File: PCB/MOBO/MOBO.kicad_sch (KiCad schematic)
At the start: 11 parts, among them J10 COMP_OUT, J103 RPi_GPio, J104 RPi_GND, J105 RPi_5V, J106 RPi_DM, J107 RPi_DM, J11 COMP_5V, J12 COMP_GND, J7 RPi_TV, J8 RPi_SDA0, J9 RPi_SCL0

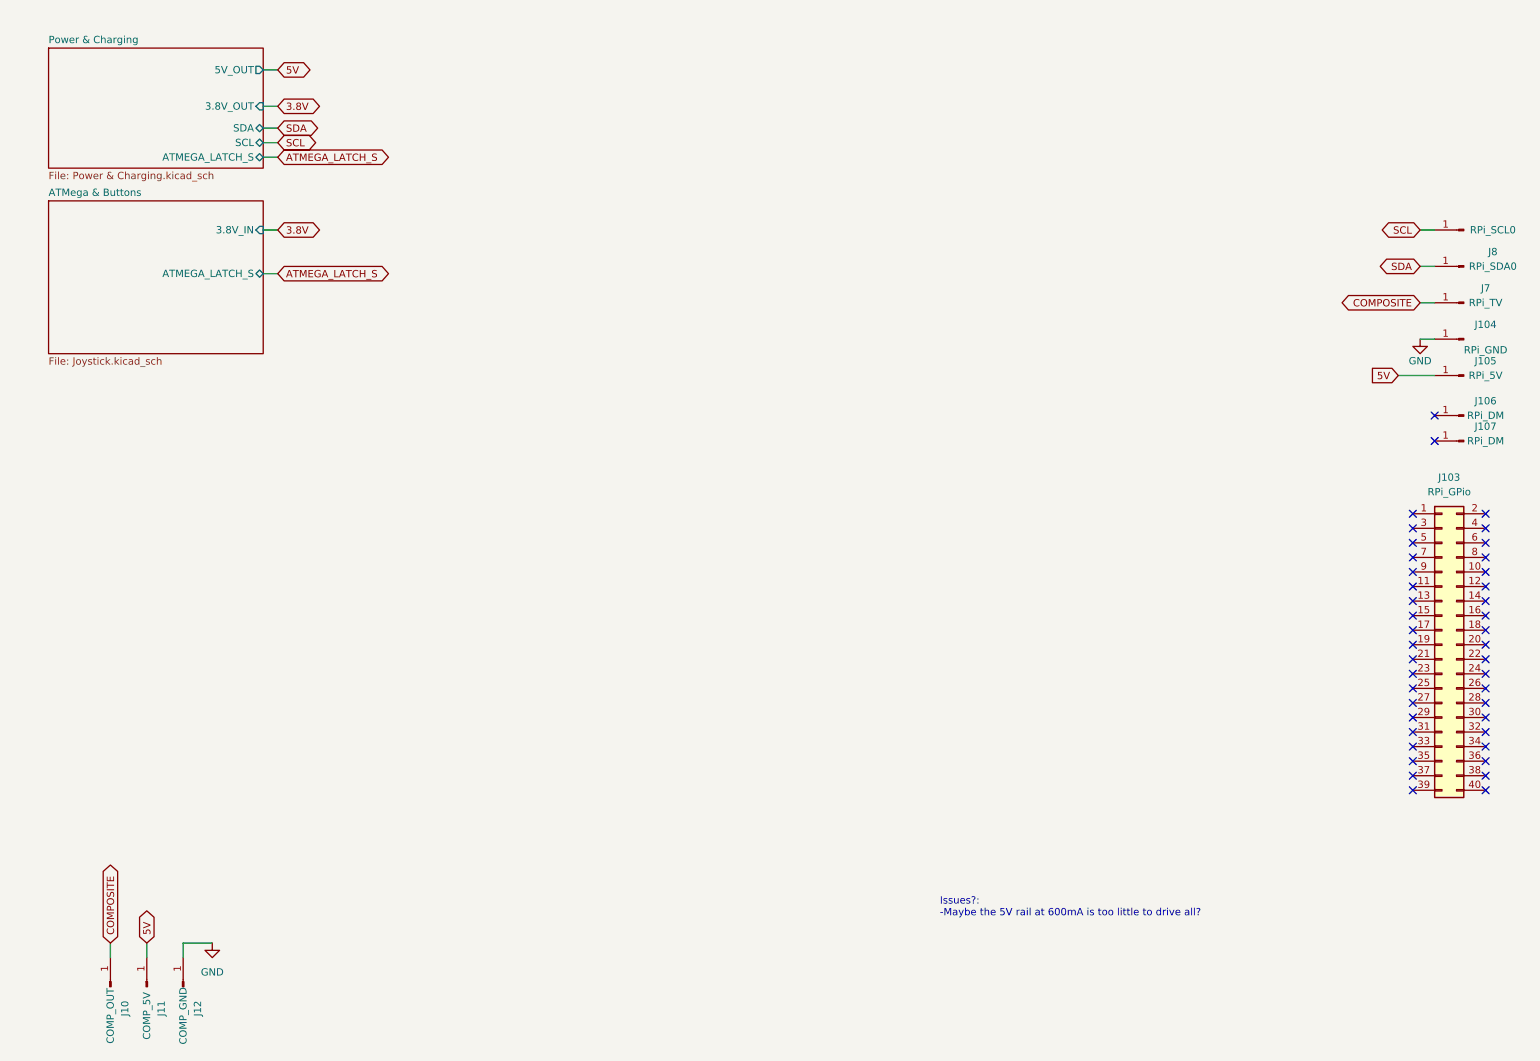
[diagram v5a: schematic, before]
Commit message: relaced usbc port schematic to add data lines
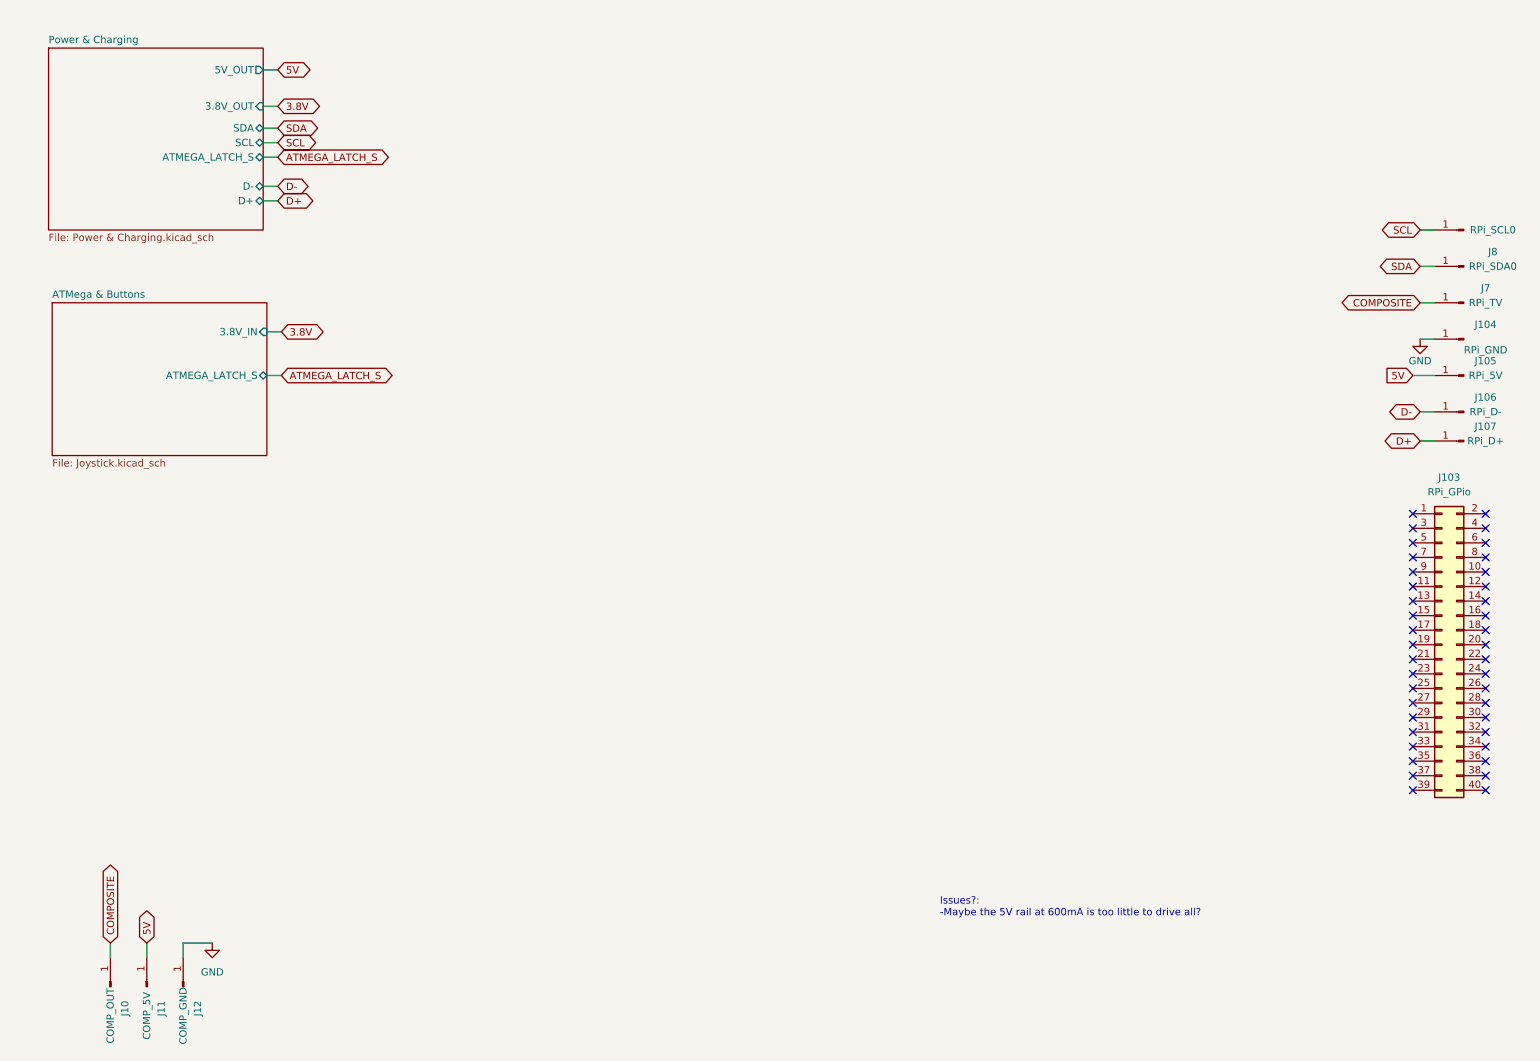
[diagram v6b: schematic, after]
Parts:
- J106: value RPi_DM -> RPi_D-
- J107: value RPi_DM -> RPi_D+
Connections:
- net D+: now reaches J107.1 (Pin_1)
- net D-: now reaches J106.1 (Pin_1)
- no-connect marks 42 -> 40
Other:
- sheet Power & Charging ports: added D+, D-; removed none
- moved on the sheet: J106
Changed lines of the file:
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@@
   (no_connect (at 260.35 107.95))
   (no_connect (at 260.35 135.89))
-  (no_connect (at 264.16 87.63))
   (no_connect (at 273.05 135.89))
   (no_connect (at 260.35 125.73))
@@
   (no_connect (at 260.35 146.05))
   (no_connect (at 260.35 113.03))
-  (no_connect (at 264.16 83.185))
   (no_connect (at 260.35 143.51))
   (no_connect (at 260.35 140.97))
@@
     (stroke (width 0) (type default))
   )
-  (wire (pts (xy 59.69 58.42) (xy 62.23 58.42))
+  (wire (pts (xy 60.325 76.2) (xy 62.865 76.2))
+    (stroke (width 0) (type default))
+  )
+  (wire (pts (xy 59.69 43.18) (xy 62.23 43.18))
+    (stroke (width 0) (type default))
+  )
+  (wire (pts (xy 264.16 87.63) (xy 261.62 87.63))
     (stroke (width 0) (type default))
   )
@@
     (stroke (width 0) (type default))
   )
+  (wire (pts (xy 264.16 82.55) (xy 261.62 82.55))
+    (stroke (width 0) (type default))
+  )
+  (wire (pts (xy 59.69 45.72) (xy 62.23 45.72))
+    (stroke (width 0) (type default))
+  )
   (wire (pts (xy 45.72 175.26) (xy 45.72 177.8))
     (stroke (width 0) (type default))
@@
     (stroke (width 0) (type default))
   )
-  (wire (pts (xy 59.69 50.8) (xy 62.23 50.8))
-    (stroke (width 0) (type default))
-  )
-  (wire (pts (xy 257.81 76.2) (xy 264.16 76.2))
+  (wire (pts (xy 260.35 76.2) (xy 264.16 76.2))
+    (stroke (width 0) (type default))
+  )
+  (wire (pts (xy 60.325 68.58) (xy 62.865 68.58))
     (stroke (width 0) (type default))
   )
@@
     )
   )
-  (global_label "ATMEGA_LATCH_S" (shape bidirectional) (at 62.23 58.42 0) (fields_autoplaced)
-    (effects (font (size 1.27 1.27)) (justify left))
-    (property "Intersheetrefs" "${INTERSHEET_REFS}" (at 82.1712 58.42 0)
+  (global_label "ATMEGA_LATCH_S" (shape bidirectional) (at 62.865 76.2 0) (fields_autoplaced)
+    (effects (font (size 1.27 1.27)) (justify left))
+    (property "Intersheetrefs" "${INTERSHEET_REFS}" (at 82.8062 76.2 0)
       (effects (font (size 1.27 1.27)) (justify left) hide)
     )
@@
     )
   )
+  (global_label "D+" (shape bidirectional) (at 62.23 45.72 0) (fields_autoplaced)
+    (effects (font (size 1.27 1.27)) (justify left))
+    (property "Intersheetrefs" "${INTERSHEET_REFS}" (at 69.1689 45.72 0)
+      (effects (font (size 1.27 1.27)) (justify left) hide)
+    )
+  )
   (global_label "COMPOSITE" (shape bidirectional) (at 33.02 175.26 90) (fields_autoplaced)
     (effects (font (size 1.27 1.27)) (justify left))
@@
     )
   )
-  (global_label "5V" (shape input) (at 257.81 76.2 180) (fields_autoplaced)
+  (global_label "5V" (shape input) (at 260.35 76.2 180) (fields_autoplaced)
     (effects (font (size 1.27 1.27)) (justify right))
-    (property "Intersheetrefs" "${INTERSHEET_REFS}" (at 252.5267 76.2 0)
+    (property "Intersheetrefs" "${INTERSHEET_REFS}" (at 255.0667 76.2 0)
       (effects (font (size 1.27 1.27)) (justify right) hide)
     )
@@
     )
   )
-  (global_label "3.8V" (shape bidirectional) (at 62.23 50.8 0) (fields_autoplaced)
-    (effects (font (size 1.27 1.27)) (justify left))
-    (property "Intersheetrefs" "${INTERSHEET_REFS}" (at 70.4389 50.8 0)
+  (global_label "3.8V" (shape bidirectional) (at 62.865 68.58 0) (fields_autoplaced)
+    (effects (font (size 1.27 1.27)) (justify left))
+    (property "Intersheetrefs" "${INTERSHEET_REFS}" (at 71.0739 68.58 0)
+      (effects (font (size 1.27 1.27)) (justify left) hide)
+    )
+  )
+  (global_label "D-" (shape bidirectional) (at 62.23 43.18 0) (fields_autoplaced)
+    (effects (font (size 1.27 1.27)) (justify left))
+    (property "Intersheetrefs" "${INTERSHEET_REFS}" (at 69.1689 43.18 0)
       (effects (font (size 1.27 1.27)) (justify left) hide)
     )
@@
     )
   )
+  (global_label "D+" (shape bidirectional) (at 261.62 87.63 180) (fields_autoplaced)
+    (effects (font (size 1.27 1.27)) (justify right))
+    (property "Intersheetrefs" "${INTERSHEET_REFS}" (at 254.6811 87.63 0)
+      (effects (font (size 1.27 1.27)) (justify right) hide)
+    )
+  )
   (global_label "SDA" (shape bidirectional) (at 62.23 33.02 0) (fields_autoplaced)
     (effects (font (size 1.27 1.27)) (justify left))
     (property "Intersheetrefs" "${INTERSHEET_REFS}" (at 69.8946 33.02 0)
       (effects (font (size 1.27 1.27)) (justify left) hide)
+    )
+  )
+  (global_label "D-" (shape bidirectional) (at 261.62 82.55 180) (fields_autoplaced)
+    (effects (font (size 1.27 1.27)) (justify right))
+    (property "Intersheetrefs" "${INTERSHEET_REFS}" (at 254.6811 82.55 0)
+      (effects (font (size 1.27 1.27)) (justify right) hide)
     )
   )
@@
       (effects (font (size 1.27 1.27)))
     )
-    (property "Value" "RPi_DM" (at 273.05 87.63 0)
+    (property "Value" "RPi_D+" (at 273.05 87.63 0)
       (effects (font (size 1.27 1.27)))
     )
@@
     )
   )
-  (symbol (lib_id "Connector:Conn_01x01_Male") (at 269.24 83.185 180) (unit 1)
-    (in_bom yes) (on_board yes) (dnp no)
-    (property "Reference" "J106" (at 273.05 80.645 0)
-      (effects (font (size 1.27 1.27)))
-    )
-    (property "Value" "RPi_DM" (at 273.05 83.185 0)
-      (effects (font (size 1.27 1.27)))
-    )
-    (property "Footprint" "TestPoint:TestPoint_Pad_1.5x1.5mm" (at 269.24 83.185 0)
-      (effects (font (size 1.27 1.27)) hide)
-    )
-    (property "Datasheet" "~" (at 269.24 83.185 0)
+  (symbol (lib_id "Connector:Conn_01x01_Male") (at 269.24 82.55 180) (unit 1)
+    (in_bom yes) (on_board yes) (dnp no)
+    (property "Reference" "J106" (at 273.05 80.01 0)
+      (effects (font (size 1.27 1.27)))
+    )
+    (property "Value" "RPi_D-" (at 273.05 82.55 0)
+      (effects (font (size 1.27 1.27)))
+    )
+    (property "Footprint" "TestPoint:TestPoint_Pad_1.5x1.5mm" (at 269.24 82.55 0)
+      (effects (font (size 1.27 1.27)) hide)
+    )
+    (property "Datasheet" "~" (at 269.24 82.55 0)
       (effects (font (size 1.27 1.27)) hide)
     )
@@
     )
   )
-  (sheet (at 22.225 45.72) (size 37.465 26.67) (fields_autoplaced)
+  (sheet (at 22.86 63.5) (size 37.465 26.67) (fields_autoplaced)
     (stroke (width 0.1524) (type solid))
     (fill (color 0 0 0 0.0000))
-    (property "Sheetname" "ATMega & Buttons" (at 22.225 45.0084 0)
+    (property "Sheetname" "ATMega & Buttons" (at 22.86 62.7884 0)
       (effects (font (size 1.27 1.27)) (justify left bottom))
     )
-    (property "Sheetfile" "Joystick.kicad_sch" (at 22.225 72.9746 0)
+    (property "Sheetfile" "Joystick.kicad_sch" (at 22.86 90.7546 0)
       (effects (font (size 1.27 1.27)) (justify left top))
     )
-    (pin "3.8V_IN" input (at 59.69 50.8 0)
-      (effects (font (size 1.27 1.27)) (justify right))
-    )
-    (pin "ATMEGA_LATCH_S" bidirectional (at 59.69 58.42 0)
+    (pin "3.8V_IN" input (at 60.325 68.58 0)
+      (effects (font (size 1.27 1.27)) (justify right))
+    )
+    (pin "ATMEGA_LATCH_S" bidirectional (at 60.325 76.2 0)
       (effects (font (size 1.27 1.27)) (justify right))
     )
@@
     )
   )
-  (sheet (at 22.225 19.05) (size 37.465 20.955) (fields_autoplaced)
+  (sheet (at 22.225 19.05) (size 37.465 31.75) (fields_autoplaced)
     (stroke (width 0.1524) (type solid))
     (fill (color 0 0 0 0.0000))
@@
       (effects (font (size 1.27 1.27)) (justify left bottom))
     )
-    (property "Sheetfile" "Power & Charging.kicad_sch" (at 22.225 40.5896 0)
+    (property "Sheetfile" "Power & Charging.kicad_sch" (at 22.225 51.3846 0)
       (effects (font (size 1.27 1.27)) (justify left top))
     )
@@
       (effects (font (size 1.27 1.27)) (justify right))
     )
+    (pin "D-" bidirectional (at 59.69 43.18 0)
+      (effects (font (size 1.27 1.27)) (justify right))
+    )
+    (pin "D+" bidirectional (at 59.69 45.72 0)
+      (effects (font (size 1.27 1.27)) (justify right))
+    )

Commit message: added connector
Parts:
- removed J104: RPi_GND, TestPoint:TestPoint_Pad_1.5x1.5mm, symbol Connector:Conn_01x01_Male
- removed J105: RPi_5V, TestPoint:TestPoint_Pad_1.5x1.5mm, symbol Connector:Conn_01x01_Male
- removed J9: RPi_SCL0, TestPoint:TestPoint_Pad_1.5x1.5mm, symbol Connector:Conn_01x01_Male
- added J105: JST_02, Connector_JST:JST_EH_B2B-EH-A_1x02_P2.50mm_Vertical, symbol PCM_SL_Connectors:JST_02
- added J110: RPi_SCL0, TestPoint:TestPoint_Pad_1.5x1.5mm, symbol Connector:Conn_01x01_Male
- renumbered J10 to J101, J11 to J102, J12 to J103, J103 to J104, J8 to J106, J7 to J107, J106 to J108, J107 to J109
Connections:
- net 5V: now also J104.2 (Pin_2)
- net GND: now also J104.6 (Pin_6), J105.2
- net SCL: now also J110.1 (Pin_1)
- new net BAT+: J105.1
- no-connect marks 40 -> 38
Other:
- sheet Power & Charging ports: added BAT+; removed none
- moved on the sheet: J106, J107
